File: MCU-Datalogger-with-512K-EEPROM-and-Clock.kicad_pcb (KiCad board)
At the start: 2 copper layers, 54.5 x 36.5 mm, 30 parts, among them J1 Conn_01x04_Pin, J2 Conn_01x04_Pin, J3 Conn_01x09_Pin, J4 Conn_02x03_Odd_Even, U1 24LC1025, U2 24LC1025, U3 ATMEGA328P-AU, U4 DS1337S_, Y1 32.768 KHz, Y2 16 MHz

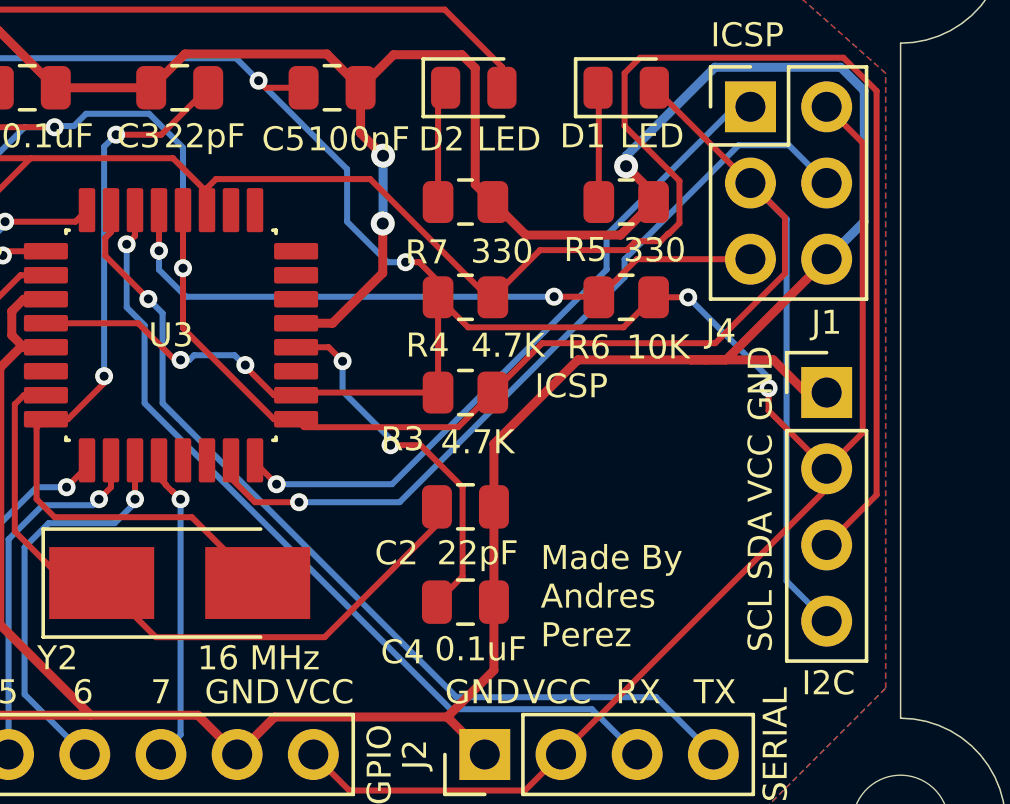
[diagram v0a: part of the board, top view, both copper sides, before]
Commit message: re-routed SCK and SCL board from new schematic
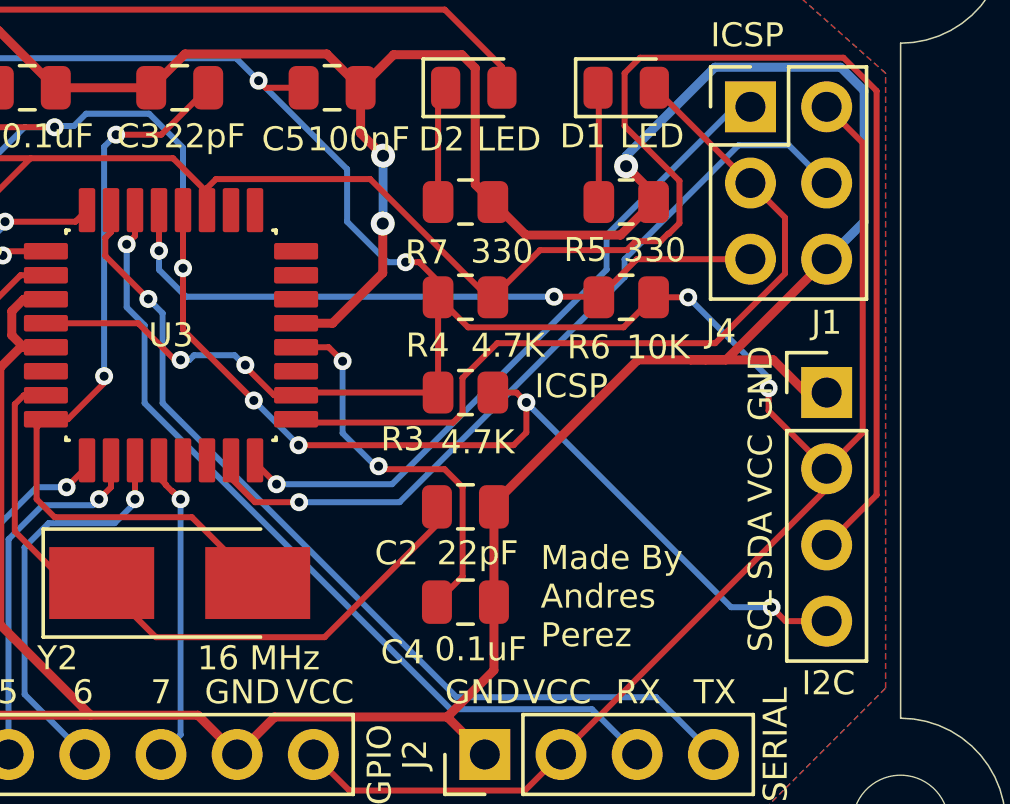
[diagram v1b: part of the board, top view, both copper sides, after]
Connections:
- D1 pad 2: /SCL -> /SCK
- J4 pad 3: /SCL -> /SCK
- U3 pad 17: /SCL -> /SCK
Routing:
- net /SCK: track 0.00 -> 27.1 mm
- net /SCL: track 83.8 -> 65.2 mm, vias 3 -> 7
- net GND: track 200.2 -> 199.1 mm
- net Net-(U3-AREF): track 12.4 -> 13.1 mm
